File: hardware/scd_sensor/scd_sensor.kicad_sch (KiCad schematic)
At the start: 2 parts, among them J5 Conn_02x10_Odd_Even, U1 SCD41-D-R2

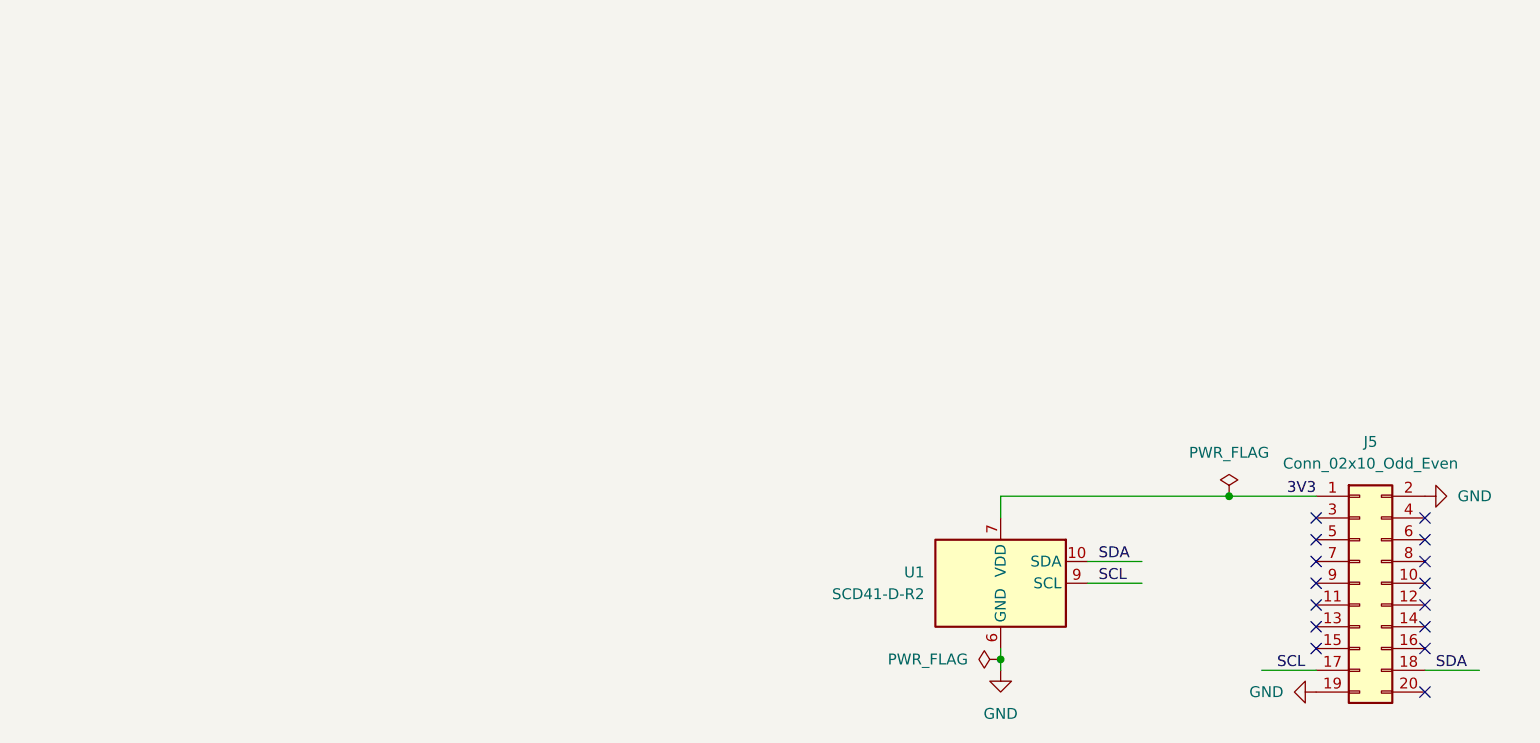
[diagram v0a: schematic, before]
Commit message: Add sensor board
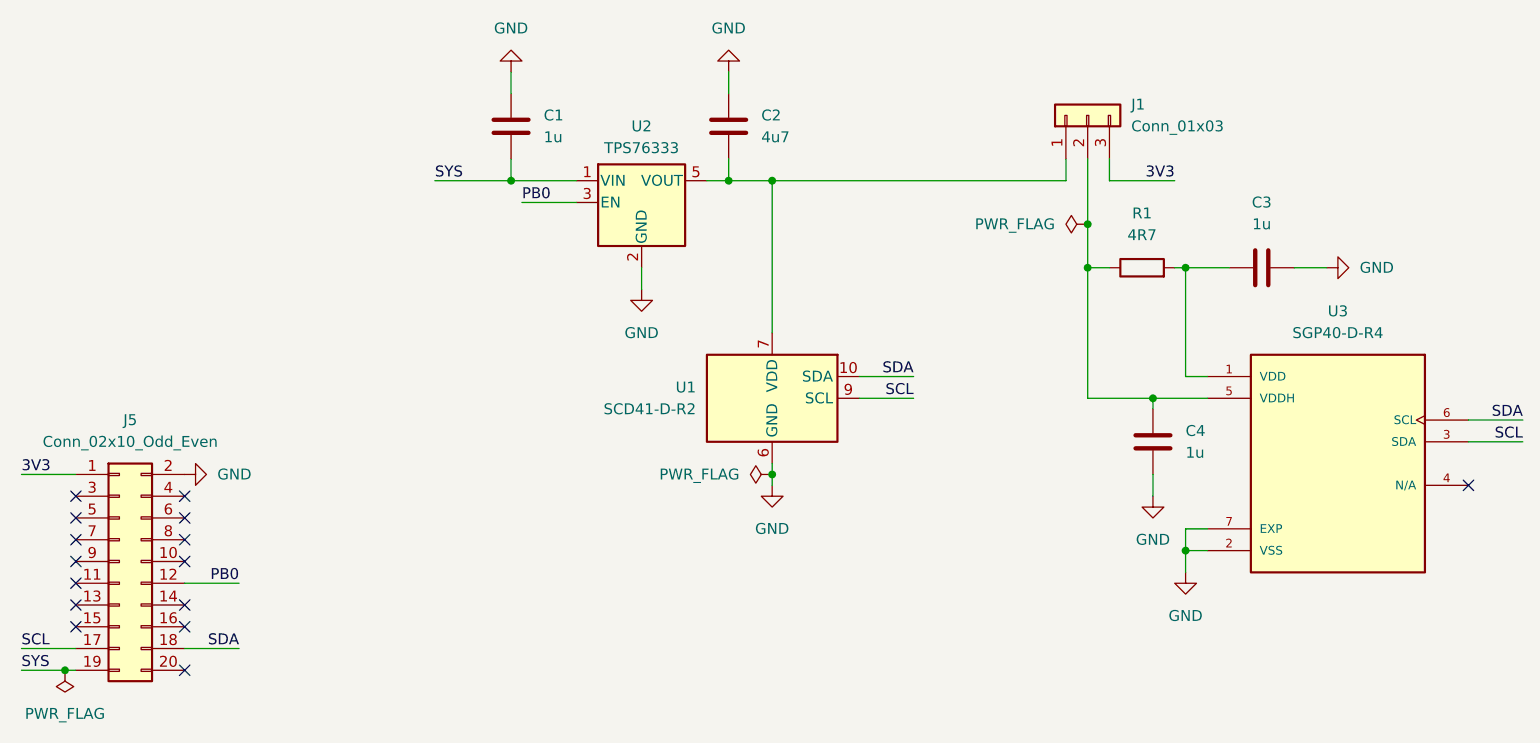
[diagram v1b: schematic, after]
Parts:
- added C1, C3, C4: 1u, Capacitor_SMD:C_0402_1005Metric, symbol Device:C
- added C2: 4u7, Capacitor_SMD:C_0402_1005Metric, symbol Device:C
- added J1: Conn_01x03, Connector_PinHeader_2.54mm:PinHeader_1x03_P2.54mm_Vertical, symbol Connector_Generic:Conn_01x03
- added R1: 4R7, Resistor_SMD:R_0402_1005Metric, symbol Device:R
- added U2: TPS76333, Package_TO_SOT_SMD:SOT-23-5, symbol Regulator_Linear:TPS76333
- added U3: SGP40-D-R4, Project_Footprints:XCDR_SGP40-D-R4, symbol Project_Symbols:SGP40-D-R4
- U1: JLCPCB C3659294 -> C3037696
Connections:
- net 3V3: now also J1.3 (Pin_3); no longer U1.19 (VDD), U1.7 (VDD)
- net GND: now also C1.1, C2.1, C3.2, C4.2, U2.2 (GND), U3.2 (VSS), U3.7 (EXP); no longer J5.19 (Pin_19)
- net SCL: now also U3.3 (SDA)
- net SDA: now also U3.6 (SCL)
- net PB0: now reaches J5.12 (Pin_12)
- net PB0: now also U2.3 (EN)
- new net: C4.1, J1.2 (Pin_2), R1.1, U3.5 (VDDH)
- new net: C2.2, J1.1 (Pin_1), U1.19 (VDD), U1.7 (VDD), U2.5 (VOUT)
- new net: C3.1, R1.2, U3.1 (VDD)
- new net SYS: C1.2, J5.19 (Pin_19), U2.1 (VIN)
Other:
- moved on the sheet: J5, U1

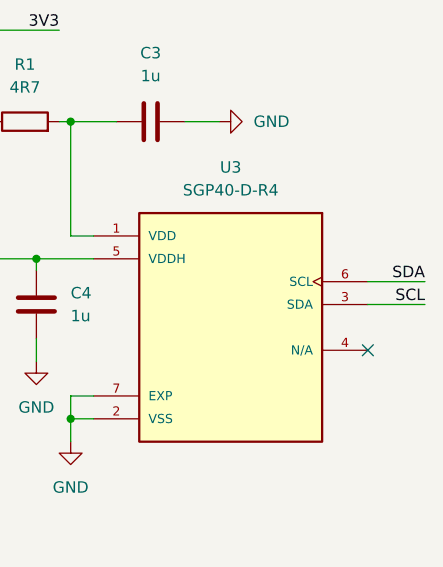
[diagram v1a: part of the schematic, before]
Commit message: Fix SDA/SCL placement on SGP40
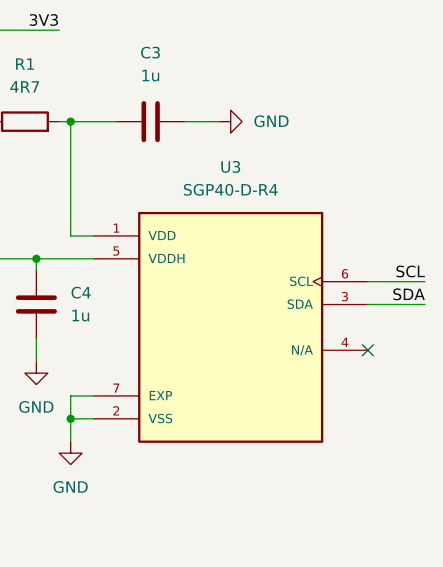
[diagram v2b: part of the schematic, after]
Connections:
- net SCL: now also U3.6 (SCL); no longer U3.3 (SDA)
- net SDA: now also U3.3 (SDA); no longer U3.6 (SCL)
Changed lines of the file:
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@@
 	)
 	(label "SDA"
-		(at 223.52 72.39 180)
+		(at 223.52 74.93 180)
 		(effects
 			(font
@@
 	)
 	(label "SCL"
-		(at 223.52 74.93 180)
+		(at 223.52 72.39 180)
 		(effects
 			(font
